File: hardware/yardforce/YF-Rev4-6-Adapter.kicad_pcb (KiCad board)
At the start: 2 copper layers, 62.3 x 70 mm, 32 parts, among them J1 USB_OTG, J2 JTAG ARM-10, J3 YF-Rev6-B, J4 YF-Rev6-A, J5 YF-Rev4-A, J6 YF-Rev4-B, J7 OM UI Board, U1 XC6220B331MR, U2 ESP32-S3-WROOM-1, U3 TCA9555PWR

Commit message: Fix DRC issues
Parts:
- added JP2: Rev4-A 3.3V, Jumper:SolderJumper-2_P1.3mm_Open_RoundedPad1.0x1.5mm, B.Cu at (171.0, 106.4)
- added JP3: Rev4-B 3.3V, Jumper:SolderJumper-2_P1.3mm_Open_RoundedPad1.0x1.5mm, F.Cu at (136.8, 61.0)
- moved R4 9.53 mm to (144.3, 71.9)
- moved R1 5.11 mm to (144.3, 68.1)
- moved R2 5.11 mm to (144.3, 69.7)
- moved C6 2.21 mm to (144.5, 62.2), turned to 180 degrees
- moved C4 1.56 mm to (142.1, 61.5), turned to -90 degrees
- moved C5 1.49 mm to (140.7, 61.6), turned to -90 degrees
- moved R7 1.08 mm to (144.2, 60.8)
- moved D1 1.00 mm to (139.4, 68.5)
- moved C3 0.80 mm to (145.5, 100.6), turned to 180 degrees
- moved J1 0.30 mm to (134.6, 68.1), turned to -90 degrees
- moved D2 0.10 mm to (144.3, 73.6)
- moved R8 0.10 mm to (147.3, 73.6)
- moved D3 0.10 mm to (144.3, 75.3)
- moved R9 0.10 mm to (147.3, 75.3)
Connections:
- J5 pad 2: /VCC (3.3V) -> Net-(J5-Pin_2)
- J5 pad 4: /JP3.06? -> unconnected-(J5-Pin_4-Pad4)
- J6 pad 2: /VCC (3.3V) -> Net-(J6-Pin_2)
- J6 pad 4: /JP3.06? -> unconnected-(J6-Pin_4-Pad4)
- U2 pad 23: unconnected-(U2-IO21-Pad23) -> /LCD_BACKLIGHT
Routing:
- net /LCD_BACKLIGHT: track 0.00 -> 69.3 mm, vias 0 -> 1
- net /LED_S2: track 15.4 -> 65.5 mm
- net Net-(J6-Pin_2): track 0.00 -> 38.3 mm
- net +3V3: track 89.7 -> 124.6 mm, vias 5 -> 8
- net /BTN_PLAY: track 179.4 -> 146.7 mm, vias 1 -> 2
- net /TXD1: track 32.8 -> 22.4 mm
- net Net-(J5-Pin_2): track 0.00 -> 9.59 mm
- net /LED_S1/ADS7843_BUSY: track 72.5 -> 66.1 mm, vias 2 -> 1
- net /RXD1: track 38.5 -> 43.5 mm
- net Net-(J1-D-): track 7.53 -> 11.4 mm
- net GND: track 10.2 -> 13.9 mm, vias 29 -> 37
- net Net-(U2-IO17): track 17.6 -> 19.5 mm
- net /LED_6H/LCD: track 73.2 -> 71.6 mm
- net /LED_8H/R1: track 75.2 -> 74.1 mm
- net Net-(D1-A): track 4.20 -> 3.32 mm
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
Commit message: BOM Update
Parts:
- C1, C2: value 10uF/10V -> 10uF
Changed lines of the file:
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@@
 			)
 		)
+		(property "JLCPCB" "C82288"
+			(at 0 0 180)
+			(unlocked yes)
+			(layer "F.Fab")
+			(hide yes)
+			(effects
+				(font
+					(size 1 1)
+					(thickness 0.15)
+				)
+			)
+		)
 		(property ki_fp_filters "TO-???* *_Diode_* *SingleDiode* D_*")
 		(sheetname "Root")
@@
 			)
 		)
-		(property "Value" "10uF/10V"
+		(property "Value" "10uF"
 			(at 0 1.43 -90)
 			(layer "F.Fab")
@@
 			)
 		)
+		(property "MF" "Espressif Systems"
+			(at 0 0 -90)
+			(unlocked yes)
+			(layer "F.Fab")
+			(hide yes)
+			(effects
+				(font
+					(size 1 1)
+					(thickness 0.15)
+				)
+			)
+		)
+		(property "MF Part" "ESP32-S3-WROOM-1-N4"
+			(at 0 0 -90)
+			(unlocked yes)
+			(layer "F.Fab")
+			(hide yes)
+			(effects
+				(font
+					(size 1 1)
+					(thickness 0.15)
+				)
+			)
+		)
+		(property "JLCPCB" "C2913197"
+			(at 0 0 -90)
+			(unlocked yes)
+			(layer "F.Fab")
+			(hide yes)
+			(effects
+				(font
+					(size 1 1)
+					(thickness 0.15)
+				)
+			)
+		)
 		(property ki_fp_filters "ESP32?S3?WROOM?1*")
 		(sheetname "Root")
@@
 		(tags "solder jumper open")
 		(property "Reference" "JP3"
-			(at 0 -1.8 360)
+			(at 0 -1.8 0)
 			(layer "F.SilkS")
 			(effects
@@
 		)
 		(property "Value" "Rev4-B 3.3V"
-			(at 0 1.9 360)
+			(at 0 1.9 0)
 			(layer "F.Fab")
 			(effects
@@
 			)
 		)
+		(property "MF" "ZHOURI"
+			(at 0 0 180)
+			(unlocked yes)
+			(layer "F.Fab")
+			(hide yes)
+			(effects
+				(font
+					(size 1 1)
+					(thickness 0.15)
+				)
+			)
+		)
+		(property "MF Part" "PZ2.54-1*2"
+			(at 0 0 180)
+			(unlocked yes)
+			(layer "F.Fab")
+			(hide yes)
+			(effects
+				(font
+					(size 1 1)
+					(thickness 0.15)
+				)
+			)
+		)
+		(property "JLCPCB" "C5360898"
+			(at 0 0 180)
+			(unlocked yes)
+			(layer "F.Fab")
+			(hide yes)
+			(effects
+				(font
+					(size 1 1)
+					(thickness 0.15)
+				)
+			)
+		)
 		(property ki_fp_filters "Jumper* TestPoint*2Pads* TestPoint*Bridge*")
 		(sheetname "Root")
@@
 			)
 		)
-		(property "Description" "USB mini/micro connector"
+		(property "Description" "1A USB 2.0 Direct Insert 5P Female, Micro-B Plugin USB"
 			(at 0 0 -90)
 			(unlocked yes)
@@
 			)
 		)
-		(property "JLCPCB" "C5454937"
+		(property "JLCPCB" "C668588"
 			(at 0 0 -90)
 			(unlocked yes)
@@
 			)
 		)
-		(property "MFR" "TYPEC-300-BCP16H65"
+		(property "MFR" "MICRO 180°ZB"
 			(at 0 0 -90)
 			(unlocked yes)
@@
 			)
 		)
-		(property "MF" "XUNPU"
+		(property "MF" "SHOU HAN"
 			(at 0 0 -90)
 			(unlocked yes)
@@
 			)
 		)
-		(property "Value" "10uF/10V"
+		(property "Value" "10uF"
 			(at 3.1625 0.55 90)
 			(layer "F.Fab")
@@
 		(tags "solder jumper open")
 		(property "Reference" "JP2"
-			(at 0 1.8 270)
+			(at 0 1.8 -90)
 			(layer "B.SilkS")
 			(effects
@@
 		)
 		(property "Value" "Rev4-A 3.3V"
-			(at 0 -1.9 270)
+			(at 0 -1.9 -90)
 			(layer "B.Fab")
 			(effects

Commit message: Add HW Prototype v0.1
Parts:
- removed C5: 10uF, Capacitor_SMD:C_0603_1608Metric
- removed JP1: Boot, Connector_PinSocket_2.54mm:PinSocket_1x02_P2.54mm_Vertical
- removed U2: ESP32-S3-WROOM-1, libs:ESP32-S3-WROOM-1_MOD
- added ?: , , F.Cu at (121.3, 52.6)
- added ANT1: 2.4Ghz, libs:PCB_Antenna_2.4GHz_Left, F.Cu at (170.3, 73.7)
- added C10: 10pF, Capacitor_SMD:C_0402_1005Metric, F.Cu at (160.4, 75.9)
- added C11: 10pF, Capacitor_SMD:C_0402_1005Metric, F.Cu at (164.3, 75.8)
- added C12: .1uF, Capacitor_SMD:C_0402_1005Metric, F.Cu at (167.2, 69.5)
- added C14: 1uF, Capacitor_SMD:C_0402_1005Metric, F.Cu at (166.4, 74.2)
- added C15: .1uF, Capacitor_SMD:C_0402_1005Metric, F.Cu at (162.0, 63.0)
- added C16: .1uF, Capacitor_SMD:C_0402_1005Metric, F.Cu at (165.4, 73.2)
- added C17: .1uF, Capacitor_SMD:C_0402_1005Metric, F.Cu at (159.8, 73.3)
- added C18: .1uF, Capacitor_SMD:C_0402_1005Metric, F.Cu at (156.2, 65.0)
- added C8: DNP, Capacitor_SMD:C_0402_1005Metric, F.Cu at (168.5, 73.8)
- added C9: 0.8pF, Capacitor_SMD:C_0402_1005Metric, F.Cu at (166.7, 71.4)
- added D4: PDZ3.3B,115, Diode_SMD:D_SOD-323, F.Cu at (136.9, 61.3)
- added GPIO33: TestPoint, TestPoint:TestPoint_Pad_1.0x1.0mm, F.Cu at (146.9, 86.3)
- added GPIO47: TestPoint, TestPoint:TestPoint_Pad_1.0x1.0mm, F.Cu at (146.9, 83.8)
- added GPIO48: TestPoint, TestPoint:TestPoint_Pad_1.0x1.0mm, F.Cu at (146.9, 81.2)
- added J8: Shell Stop, Connector_JST:JST_XH_B3B-XH-A_1x03_P2.50mm_Vertical, F.Cu at (136.1, 105.0)
- added J9: Rain, Connector_JST:JST_XH_B2B-XH-A_1x02_P2.50mm_Vertical, F.Cu at (139.0, 65.3)
- added L1: 3.9nH, Inductor_SMD:L_0402_1005Metric, F.Cu at (168.1, 72.1)
- added L2: 2.0nH, Inductor_SMD:L_0402_1005Metric, F.Cu at (168.4, 68.0)
- added L3: 24nH, Inductor_SMD:L_0402_1005Metric, F.Cu at (163.2, 73.3)
- added R12: 10k, Resistor_SMD:R_0603_1608Metric, F.Cu at (140.3, 60.5)
- added REF**: JLCPCB_ToolingHole_1.152mm, libs:JLCPCB_ToolingHole_1.152mm, F.Cu at (121.2, 117.4)
- added REF**: JLCPCB_ToolingHole_1.152mm, libs:JLCPCB_ToolingHole_1.152mm, F.Cu at (174.6, 52.6)
- added S1: RST, libs:SW_TS-1187A-B-A-B, F.Cu at (162.8, 80.5)
- added U4: ESP32-S3-FH4R2, Package_DFN_QFN:QFN-56-1EP_7x7mm_P0.4mm_EP4x4mm_ThermalVias, F.Cu at (161.4, 68.1)
- added Y1: 40MHz 10.5pF ±10ppm, Crystal:Crystal_SMD_2016-4Pin_2.0x1.6mm, F.Cu at (162.3, 75.6)
- J2: value JTAG ARM-10 -> TC2050-IDC; footprint Connector_IDC:IDC-Header_2x05_P2.54mm_Vertical -> libs:TAG-CONNECT_TC2050-IDC
- JP3: moved to B.Cu
- R1, R2: footprint Resistor_SMD:R_0603_1608Metric -> Resistor_SMD:R_0402_1005Metric
- R8: value 180 -> 200
- U1: value XC6220B331MR -> AMS1117-3.3; footprint Package_TO_SOT_SMD:SOT-23-5 -> Package_TO_SOT_SMD:SOT-223-3_TabPin2
- moved JP3 31.0 mm to (167.8, 61.5), turned to -90 degrees
- moved R7 29.9 mm to (167.6, 79.5), turned to -90 degrees
- moved C6 29.9 mm to (168.9, 79.5), turned to -90 degrees
- moved R4 17.7 mm to (157.8, 60.5)
- moved R2 15.2 mm to (158.0, 63.2)
- moved R1 14.9 mm to (158.0, 62.1)
- moved J1 12.3 mm to (146.5, 64.9)
- moved R5 10.7 mm to (156.6, 78.1), turned to 180 degrees
- moved R3 10.7 mm to (156.7, 73.8)
- moved J2 9.72 mm to (163.5, 90.3), turned to 180 degrees
- moved D1 8.95 mm to (146.9, 73.3), turned to 0 degrees
- moved J7 3.25 mm to (159.7, 99.6), turned to 0 degrees
- moved C1 2.85 mm to (155.1, 104.6)
- moved D2 2.58 mm to (145.5, 75.9)
- moved R8 2.58 mm to (148.5, 75.9)
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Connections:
- C4 pad 1: +3V3 -> Net-(D4-K)
- J1 pad 2: Net-(J1-D-) -> /USB_D-
- J1 pad 3: Net-(J1-D+) -> /USB_D+
- J2 pad 10: /JTAG_NRST -> unconnected-(J2-Pad10)
- R1 pad 1: /USB_D- -> Net-(U4-GPIO19/USB_D-/ADC2_CH8)
- R1 pad 2: Net-(J1-D-) -> /USB_D-
- R2 pad 1: /USB_D+ -> Net-(U4-GPIO20/USB_D+/ADC2_CH9)
- R2 pad 2: Net-(J1-D+) -> /USB_D+
- U1 pad 1: +5V -> GND
- U1 pad 2: GND -> +3V3
- U3 pad 11: /BTN_PLAY -> /Shell Stop 1
- U3 pad 20: unconnected-(U3-P17-Pad20) -> /Shell Stop 2
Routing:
- net Net-(J6-Pin_2): track 38.3 -> 6.05 mm
- net /TXD1: track 22.4 -> 48.6 mm
- net /RAIN: track 0.00 -> 24.9 mm
- net +3V3: track 124.6 -> 148.8 mm, vias 8 -> 14
- net Net-(U4-GPIO33): track 0.00 -> 23.5 mm
- net /BTN_PLAY: track 146.7 -> 170.0 mm, vias 2 -> 1
- net Net-(U4-SPICLK_P/GPIO47): track 0.00 -> 21.5 mm
- net /JTAG_TDI: track 9.15 -> 30.4 mm, vias 0 -> 2
- net Net-(U4-SPICLK_N/GPIO48): track 0.00 -> 19.4 mm
- net /LED_4H/LCD: track 63.5 -> 78.3 mm
- net /JTAG_TCK-SWCLK: track 9.43 -> 23.9 mm, vias 0 -> 2
- net Net-(U4-GPIO17/ADC2_CH6): track 19.5 -> 5.09 mm
- net /JTAG_TDO-SWD: track 8.43 -> 21.7 mm
- net /LED_RD: track 2.15 -> 15.3 mm
- net /~{PE_INT}: track 25.7 -> 38.4 mm
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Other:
- outline, holes or cut-outs redrawn
- board text added: "JLCJLCJLCJLC"
- board text added: "YardForce Rev4-6 CoverUI-Adapter v0.1"

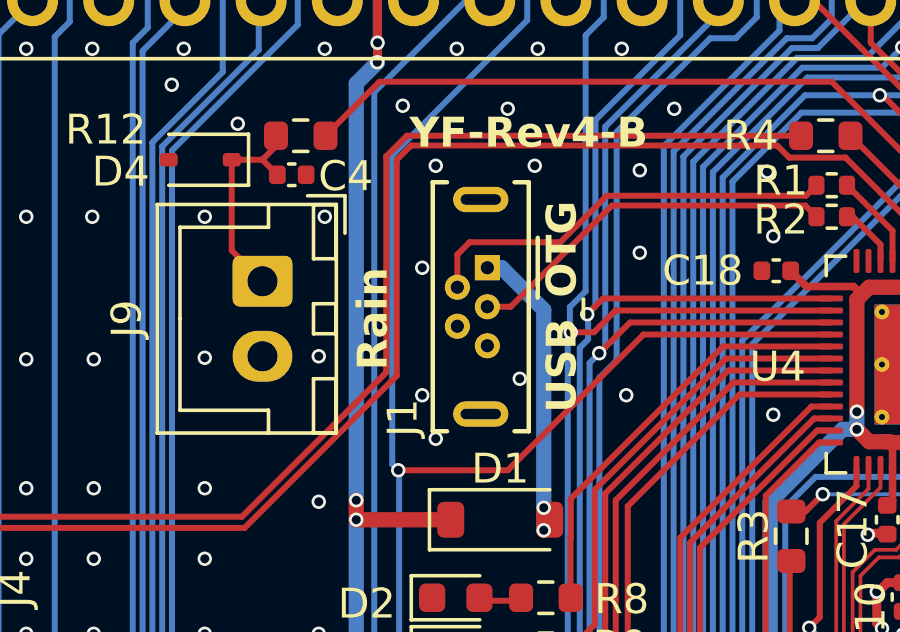
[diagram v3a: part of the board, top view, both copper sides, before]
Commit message: Change Micro-USB part to U255-051N-4BH70-SS
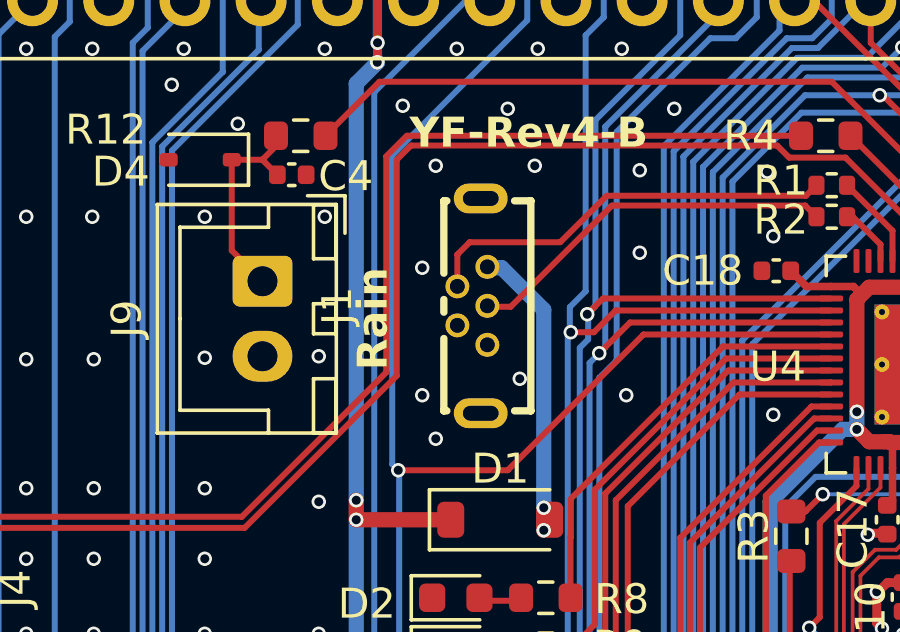
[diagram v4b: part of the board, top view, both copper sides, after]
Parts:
- J1: footprint libs:USB_Micro-B_Wuerth_614105150721_Vertical -> libs:MINI-USB-SMD_U255-051N-4BH70-XS
- moved J1 1.36 mm to (146.0, 66.2), turned to 90 degrees
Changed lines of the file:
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@@
 		(sheetname "Root")
 		(sheetfile "YF-Rev4-6-Adapter.kicad_sch")
-		(attr through_hole exclude_from_pos_files exclude_from_bom dnp)
+		(attr through_hole exclude_from_pos_files)
 		(fp_line
 			(start 7.08 2.78)
@@
 		(sheetname "Root")
 		(sheetfile "YF-Rev4-6-Adapter.kicad_sch")
-		(attr through_hole exclude_from_pos_files exclude_from_bom dnp)
+		(attr through_hole exclude_from_pos_files)
 		(fp_line
 			(start 7.08 2.78)
@@
 		(sheetname "Root")
 		(sheetfile "YF-Rev4-6-Adapter.kicad_sch")
-		(attr through_hole exclude_from_pos_files exclude_from_bom dnp)
+		(attr through_hole exclude_from_pos_files)
 		(fp_line
 			(start 52.05 1.8)
@@
 		)
 	)
-	(footprint "libs:USB_Micro-B_Wuerth_614105150721_Vertical"
+	(footprint "libs:MINI-USB-SMD_U255-051N-4BH70-XS"
 		(layer "F.Cu")
-		(at 146.52 64.9 -90)
-		(descr "USB Micro-B receptacle, through-hole, vertical, http://katalog.we-online.de/em/datasheet/614105150721.pdf")
-		(tags "usb micro receptacle vertical")
+		(at 146.02 66.17 90)
 		(property "Reference" "J1"
-			(at 5 2.82 90)
+			(at 0 -4.5 270)
 			(layer "F.SilkS")
 			(effects
@@
 		)
 		(property "Value" "USB_OTG"
-			(at 1.3 -2.48 90)
-			(layer "F.SilkS")
+			(at 0 4.5 270)
+			(layer "F.Fab")
 			(effects
 				(font
 					(size 1 1)
-					(thickness 0.2)
-					(bold yes)
+					(thickness 0.15)
 				)
 			)
 		)
-		(property "Footprint" "libs:USB_Micro-B_Wuerth_614105150721_Vertical"
-			(at 0 0 -90)
+		(property "Footprint" "libs:MINI-USB-SMD_U255-051N-4BH70-XS"
+			(at 0 0 90)
 			(unlocked yes)
 			(layer "F.Fab")
@@
 		)
 		(property "Datasheet" " ~"
-			(at 0 0 -90)
+			(at 0 0 90)
 			(unlocked yes)
 			(layer "F.Fab")
@@
 			)
 		)
-		(property "Description" "1A USB 2.0 Direct Insert 5P Female, Micro-B Plugin USB"
-			(at 0 0 -90)
+		(property "Description" "USB 2.0 1.8A 1 235℃ Direct Insert 5P Female -40℃~+85℃ Gold Brass Alloy Micro-B Plugin USB Connectors"
+			(at 0 0 90)
 			(unlocked yes)
 			(layer "F.Fab")
@@
 			)
 		)
-		(property "JLCPCB" ""
-			(at 0 0 -90)
-			(unlocked yes)
-			(layer "F.Fab")
-			(hide yes)
-			(effects
-				(font
-					(size 1 1)
-					(thickness 0.15)
-				)
-			)
-		)
-		(property "MFR" "MICRO 180°ZB"
-			(at 0 0 -90)
+		(property "MFR" "U255-051N-4BH70-SS"
+			(at 0 0 90)
 			(unlocked yes)
 			(layer "F.Fab")
@@
 			)
 		)
-		(property "MF" "SHOU HAN"
-			(at 0 0 -90)
+		(property "MF" "XKB Connection"
+			(at 0 0 90)
 			(unlocked yes)
 			(layer "F.Fab")
@@
 			)
 		)
-		(property "LCSC" "C668588"
-			(at 0 0 -90)
+		(property "LCSC" "C437033"
+			(at 0 0 90)
 			(unlocked yes)
 			(layer "F.Fab")
@@
 		(sheetname "Root")
 		(sheetfile "YF-Rev4-6-Adapter.kicad_sch")
-		(attr through_hole)
+		(attr smd)
 		(fp_line
-			(start -2.85 1.82)
-			(end 5.45 1.82)
+			(start 3.5 -0.95)
+			(end 3.5 -0.85)
 			(stroke
-				(width 0.15)
+				(width 0.25)
 				(type solid)
 			)
@@
 		)
 		(fp_line
-			(start 5.45 1.82)
-			(end 5.45 1.345)
+			(start 1.09 -0.95)
+			(end 3.5 -0.95)
 			(stroke
-				(width 0.15)
+				(width 0.25)
 				(type solid)
 			)
@@
 		)
 		(fp_line
-			(start -2.85 1.345)
-			(end -2.85 1.82)
+			(start -0.21 -0.95)
+			(end 0.21 -0.95)
 			(stroke
-				(width 0.15)
+				(width 0.25)
 				(type solid)
 			)
@@
 		)
 		(fp_line
-			(start -2.85 -0.905)
-			(end -2.85 -1.38)
+			(start -3.5 -0.95)
+			(end -1.09 -0.95)
 			(stroke
-				(width 0.15)
+				(width 0.25)
 				(type solid)
 			)
@@
 		)
 		(fp_line
-			(start -2.85 -1.38)
-			(end 5.45 -1.38)
+			(start -3.5 -0.95)
+			(end -3.5 -0.85)
 			(stroke
-				(width 0.15)
+				(width 0.25)
 				(type solid)
 			)
@@
 		)
 		(fp_line
-			(start 5.45 -1.38)
-			(end 5.45 -0.905)
+			(start 3.5 1.41)
+			(end 3.5 1.95)
 			(stroke
-				(width 0.15)
+				(width 0.25)
 				(type solid)
 			)
@@
 		)
 		(fp_line
-			(start -1 -1.68)
-			(end 1 -1.68)
+			(start -3.5 1.41)
+			(end -3.5 1.95)
 			(stroke
-				(width 0.15)
+				(width 0.25)
 				(type solid)
 			)
@@
 		)
 		(fp_line
-			(start -3.2 2.17)
-			(end 5.8 2.17)
-			(stroke
-				(width 0.05)
-				(type solid)
-			)
-			(layer "F.CrtYd")
-		)
-		(fp_line
-			(start 5.8 2.17)
-			(end 5.8 -1.73)
+			(start 3.5 1.95)
+			(end -3.5 1.95)
 			(stroke
-				(width 0.05)
+				(width 0.25)
 				(type solid)
 			)
-			(layer "F.CrtYd")
-		)
-		(fp_line
-			(start -3.2 -1.73)
-			(end -3.2 2.17)
-			(stroke
-				(width 0.05)
-				(type solid)
-			)
-			(layer "F.CrtYd")
-		)
-		(fp_line
-			(start 5.8 -1.73)
-			(end -3.2 -1.73)
-			(stroke
-				(width 0.05)
-				(type solid)
-			)
-			(layer "F.CrtYd")
-		)
-		(fp_line
-			(start -2.7 1.67)
-			(end -2.7 -1.23)
-			(stroke
-				(width 0.15)
-				(type solid)
-			)
-			(layer "F.Fab")
+			(layer "F.SilkS")
 		)
-		(fp_line
-			(start 5.3 1.67)
-			(end -2.7 1.67)
+		(fp_circle
+			(center 0.65 -0.5)
+			(end 0.73 -0.5)
 			(stroke
 				(width 0.15)
 				(type solid)
 			)
+			(fill none)
 			(layer "F.Fab")
 		)
-		(fp_line
-			(start 0 -0.23)
-			(end 1 -1.23)
+		(fp_circle
+			(center -0.65 -0.5)
+			(end -0.57 -0.5)
 			(stroke
 				(width 0.15)
 				(type solid)
 			)
+			(fill none)
 			(layer "F.Fab")
 		)
-		(fp_line
-			(start -2.7 -1.23)
-			(end -1 -1.23)
+		(fp_circle
+			(center 1.3 0.5)
+			(end 1.38 0.5)
 			(stroke
 				(width 0.15)
 				(type solid)
 			)
+			(fill none)
 			(layer "F.Fab")
 		)
-		(fp_line
-			(start -1 -1.23)
-			(end 0 -0.23)
+		(fp_circle
+			(center 0 0.5)
+			(end 0.08 0.5)
 			(stroke
 				(width 0.15)
 				(type solid)
 			)
+			(fill none)
 			(layer "F.Fab")
 		)
-		(fp_line
-			(start 1 -1.23)
-			(end 5.3 -1.23)
+		(fp_circle
+			(center -1.3 0.5)
+			(end -1.22 0.5)
 			(stroke
 				(width 0.15)
 				(type solid)
 			)
+			(fill none)
 			(layer "F.Fab")
 		)
-		(fp_line
-			(start 5.3 -1.23)
-			(end 5.3 1.67)
+		(fp_circle
+			(center 4.08 2.08)
+			(end 4.11 2.08)
 			(stroke
-				(width 0.15)
+				(width 0.06)
 				(type solid)
 			)
+			(fill none)
 			(layer "F.Fab")
 		)
 		(fp_text user "${REFERENCE}"
-			(at 1.3 0.22 90)
+			(at 0 0 270)
 			(layer "F.Fab")
 			(effects
@@
 			)
 		)
-		(pad "1" thru_hole rect
-			(at 0 0 270)
-			(size 0.84 0.84)
-			(drill 0.44)
+		(pad "1" thru_hole circle
+			(at 1.3 0.5 270)
+			(size 0.8 0.8)
+			(drill 0.500024)
 			(layers "*.Cu" "*.Mask")
 			(remove_unused_layers no)
@@
 		)
 		(pad "2" thru_hole circle
-			(at 0.65 1 270)
-			(size 0.84 0.84)
-			(drill 0.44)
+			(at 0.65 -0.5 270)
+			(size 0.8 0.8)
+			(drill 0.500024)
 			(layers "*.Cu" "*.Mask")
 			(remove_unused_layers no)
@@
 		)
 		(pad "3" thru_hole circle
-			(at 1.3 0 270)
-			(size 0.84 0.84)
-			(drill 0.44)
+			(at 0 0.5 270)
+			(size 0.8 0.8)
+			(drill 0.500024)
 			(layers "*.Cu" "*.Mask")
 			(remove_unused_layers no)
@@
 		)
 		(pad "4" thru_hole circle
-			(at 1.95 1 270)
-			(size 0.84 0.84)
-			(drill 0.44)
+			(at -0.65 -0.5 270)
+			(size 0.8 0.8)
+			(drill 0.500024)
 			(layers "*.Cu" "*.Mask")
 			(remove_unused_layers no)
@@
 		)
 		(pad "5" thru_hole circle
-			(at 2.6 0 270)
-			(size 0.84 0.84)
-			(drill 0.44)
+			(at -1.3 0.5 270)
+			(size 0.8 0.8)
+			(drill 0.500024)
 			(layers "*.Cu" "*.Mask")
 			(remove_unused_layers no)
@@
 		)
 		(pad "6" thru_hole oval
-			(at -2.275 0.22 270)
-			(size 0.85 1.85)
-			(drill oval 0.35 1.35)
+			(at -3.58 0.28)
+			(size 1.8 1)
+			(drill oval 1.199998 0.500024)
 			(layers "*.Cu" "*.Mask")
 			(remove_unused_layers no)
@@
 		)
 		(pad "6" thru_hole oval
-			(at 4.875 0.22 270)
-			(size 0.85 1.85)
-			(drill oval 0.35 1.35)
+			(at 3.58 0.28)
+			(size 1.8 1)
+			(drill oval 1.199998 0.500024)
 			(layers "*.Cu" "*.Mask")
 			(remove_unused_layers no)
@@
 			(pintype "passive")
 		)
-		(model "${KICAD8_3DMODEL_DIR}/Connector_USB.3dshapes/USB_Micro-B_Wuerth_614105150721_Vertical.wrl"
+		(model "./MICRO-USB-TH_MICRO-USB-A14.wrl"
 			(offset
 				(xyz 0 0 0)
@@
 			)
 		)
-		(model "${KIPRJMOD}/libs/USB_Micro-B_Wuerth_614105150721_Vertical.step"
-			(offset
-				(xyz 1.3 -0.1 0)
-			)
-			(scale
-				(xyz 1 0.9 1)
-			)
-			(rotate
-				(xyz 90 0 0)
-			)
-		)
 	)
 	(footprint "Package_SO:TSSOP-24_4.4x7.8mm_P0.65mm"
@@
 		(sheetname "Root")
 		(sheetfile "YF-Rev4-6-Adapter.kicad_sch")
-		(attr through_hole exclude_from_pos_files exclude_from_bom dnp)
+		(attr through_hole exclude_from_pos_files)
 		(fp_line
 			(start 52.05 1.8)
